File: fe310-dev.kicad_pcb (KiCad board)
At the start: 2 copper layers, 50 x 50 mm, 42 parts, among them J1 USB_B_Mini, J2 Conn_01x06, J3 Conn_01x12, J4 Conn_01x12, J5 Conn_01x08, SW1 SW_Push, U1 AMS1117-3.3, U2 AMS1117-1.8, U3 HT42B534, U4 FE310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

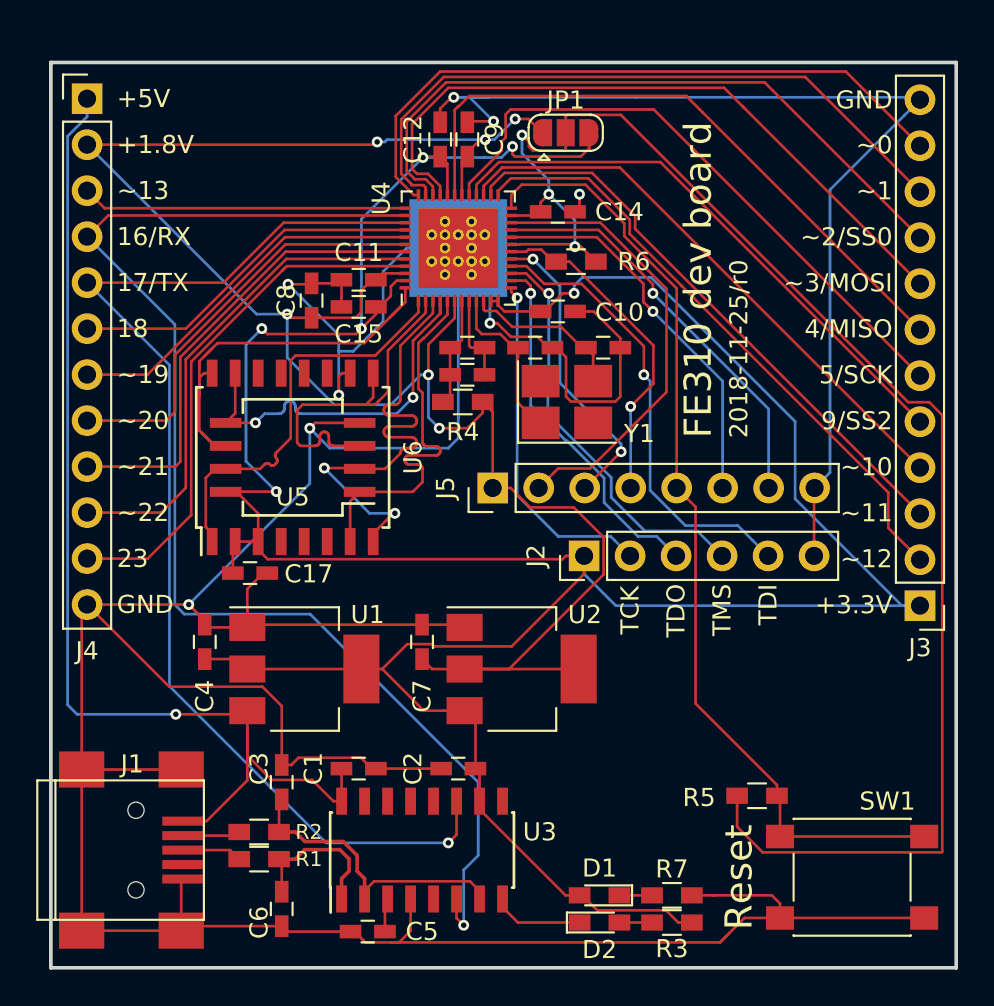
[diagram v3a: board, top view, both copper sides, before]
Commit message: various fixes and updates to silkscreen, closes #1 and #2
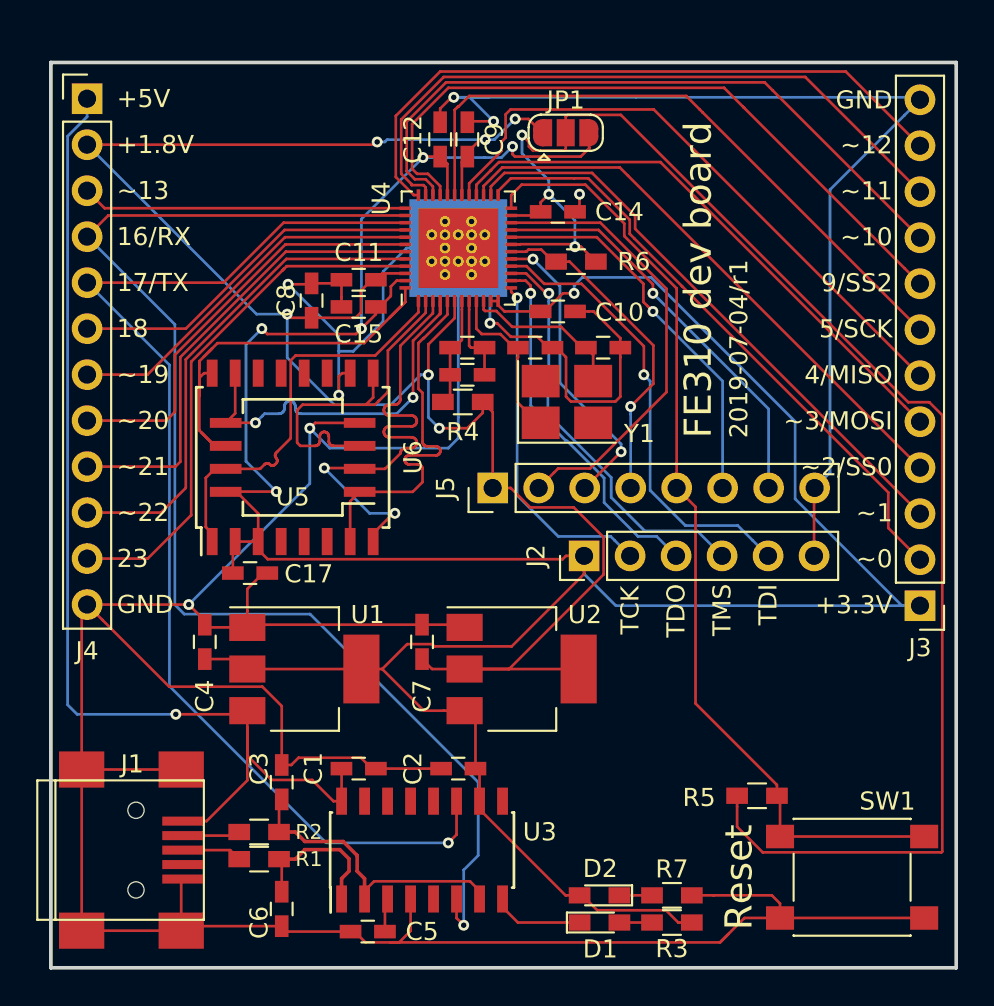
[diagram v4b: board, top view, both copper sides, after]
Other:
- board text added: "2019-07-04/r1"
- board text removed: "2018-11-25/r0"
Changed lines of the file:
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@@
     (tags "LED 0603")
     (attr smd)
-    (fp_text reference D1 (at 0 -3) (layer F.SilkS)
+    (fp_text reference D1 (at 0.039 1.467) (layer F.SilkS)
       (effects (font (size 1 1) (thickness 0.15)))
     )
@@
       (effects (font (size 1 1) (thickness 0.15)))
     )
+    (fp_line (start -1.8 -0.55) (end -1.8 0.55) (layer F.SilkS) (width 0.12))
+    (fp_line (start -0.2 -0.2) (end -0.2 0.2) (layer F.Fab) (width 0.1))
+    (fp_line (start -0.15 0) (end 0.15 -0.2) (layer F.Fab) (width 0.1))
+    (fp_line (start 0.15 0.2) (end -0.15 0) (layer F.Fab) (width 0.1))
+    (fp_line (start 0.15 -0.2) (end 0.15 0.2) (layer F.Fab) (width 0.1))
+    (fp_line (start 0.8 0.4) (end -0.8 0.4) (layer F.Fab) (width 0.1))
+    (fp_line (start 0.8 -0.4) (end 0.8 0.4) (layer F.Fab) (width 0.1))
+    (fp_line (start -0.8 -0.4) (end 0.8 -0.4) (layer F.Fab) (width 0.1))
+    (fp_line (start -1.8 0.55) (end 0.8 0.55) (layer F.SilkS) (width 0.12))
+    (fp_line (start -1.8 -0.55) (end 0.8 -0.55) (layer F.SilkS) (width 0.12))
+    (fp_line (start -1.96 -0.7) (end 1.95 -0.7) (layer F.CrtYd) (width 0.05))
+    (fp_line (start -1.96 -0.7) (end -1.96 0.7) (layer F.CrtYd) (width 0.05))
+    (fp_line (start 1.95 0.7) (end 1.95 -0.7) (layer F.CrtYd) (width 0.05))
+    (fp_line (start 1.95 0.7) (end -1.96 0.7) (layer F.CrtYd) (width 0.05))
     (fp_line (start -0.8 -0.4) (end -0.8 0.4) (layer F.Fab) (width 0.1))
-    (fp_line (start 1.95 0.7) (end -1.96 0.7) (layer F.CrtYd) (width 0.05))
-    (fp_line (start 1.95 0.7) (end 1.95 -0.7) (layer F.CrtYd) (width 0.05))
-    (fp_line (start -1.96 -0.7) (end -1.96 0.7) (layer F.CrtYd) (width 0.05))
-    (fp_line (start -1.96 -0.7) (end 1.95 -0.7) (layer F.CrtYd) (width 0.05))
-    (fp_line (start -1.8 -0.55) (end 0.8 -0.55) (layer F.SilkS) (width 0.12))
-    (fp_line (start -1.8 0.55) (end 0.8 0.55) (layer F.SilkS) (width 0.12))
-    (fp_line (start -0.8 -0.4) (end 0.8 -0.4) (layer F.Fab) (width 0.1))
-    (fp_line (start 0.8 -0.4) (end 0.8 0.4) (layer F.Fab) (width 0.1))
-    (fp_line (start 0.8 0.4) (end -0.8 0.4) (layer F.Fab) (width 0.1))
-    (fp_line (start 0.15 -0.2) (end 0.15 0.2) (layer F.Fab) (width 0.1))
-    (fp_line (start 0.15 0.2) (end -0.15 0) (layer F.Fab) (width 0.1))
-    (fp_line (start -0.15 0) (end 0.15 -0.2) (layer F.Fab) (width 0.1))
-    (fp_line (start -0.2 -0.2) (end -0.2 0.2) (layer F.Fab) (width 0.1))
-    (fp_line (start -1.8 -0.55) (end -1.8 0.55) (layer F.SilkS) (width 0.12))
+    (pad 1 smd rect (at -1.1 0) (size 1.2 0.9) (layers F.Cu F.Paste F.Mask)
+      (net 11 "Net-(D1-Pad1)"))
     (pad 2 smd rect (at 1.1 0) (size 1.2 0.9) (layers F.Cu F.Paste F.Mask)
       (net 10 "Net-(D1-Pad2)"))
-    (pad 1 smd rect (at -1.1 0) (size 1.2 0.9) (layers F.Cu F.Paste F.Mask)
-      (net 11 "Net-(D1-Pad1)"))
     (model ${KISYS3DMOD}/LEDs.3dshapes/LED_0603.wrl
       (at (xyz 0 0 0))
@@
     (tags "LED 0603")
     (attr smd)
-    (fp_text reference D2 (at 0 -3 180) (layer F.SilkS)
+    (fp_text reference D2 (at -0.039 1.478 180) (layer F.SilkS)
       (effects (font (size 1 1) (thickness 0.15)))
     )
@@
       (net 52 +VAON))
   )
-  (gr_text 2018-11-25/r0 (at 58 35.75 90) (layer F.SilkS)
+  (gr_text 2019-07-04/r1 (at 58 35.75 90) (layer F.SilkS)
     (effects (font (size 1 1) (thickness 0.25)) (justify left))
   )
@@
     (effects (font (size 1 1) (thickness 0.25)) (justify left))
   )
-  (gr_text ~~12 (at 66.486 42.418) (layer F.SilkS)
-    (effects (font (size 1 1) (thickness 0.25)) (justify right))
-  )
-  (gr_text ~~11 (at 66.486 39.878) (layer F.SilkS)
-    (effects (font (size 1 1) (thickness 0.25)) (justify right))
-  )
-  (gr_text ~~10 (at 66.486 37.338) (layer F.SilkS)
-    (effects (font (size 1 1) (thickness 0.25)) (justify right))
-  )
-  (gr_text 9/SS2 (at 66.486 34.798) (layer F.SilkS)
-    (effects (font (size 1 1) (thickness 0.25)) (justify right))
-  )
-  (gr_text 5/SCK (at 66.486 32.258) (layer F.SilkS)
-    (effects (font (size 1 1) (thickness 0.25)) (justify right))
-  )
-  (gr_text 4/MISO (at 66.486 29.718) (layer F.SilkS)
-    (effects (font (size 1 1) (thickness 0.25)) (justify right))
-  )
-  (gr_text ~~3/MOSI (at 66.486 27.178) (layer F.SilkS)
-    (effects (font (size 1 1) (thickness 0.25)) (justify right))
-  )
-  (gr_text ~~2/SS0 (at 66.486 24.638) (layer F.SilkS)
-    (effects (font (size 1 1) (thickness 0.25)) (justify right))
-  )
-  (gr_text ~~1 (at 66.486 22.098) (layer F.SilkS)
-    (effects (font (size 1 1) (thickness 0.25)) (justify right))
-  )
-  (gr_text ~~0 (at 66.486 19.558) (layer F.SilkS)
-    (effects (font (size 1 1) (thickness 0.25)) (justify right))
-  )
+  (gr_text ~~0 (at 66.486 42.418) (layer F.SilkS)
+    (effects (font (size 1 1) (thickness 0.25)) (justify right))
+  )
+  (gr_text ~~1 (at 66.486 39.878) (layer F.SilkS)
+    (effects (font (size 1 1) (thickness 0.25)) (justify right))
+  )
+  (gr_text ~~2/SS0 (at 66.486 37.338) (layer F.SilkS)
+    (effects (font (size 1 1) (thickness 0.25)) (justify right))
+  )
+  (gr_text ~~3/MOSI (at 66.486 34.798) (layer F.SilkS)
+    (effects (font (size 1 1) (thickness 0.25)) (justify right))
+  )
+  (gr_text 4/MISO (at 66.486 32.258) (layer F.SilkS)
+    (effects (font (size 1 1) (thickness 0.25)) (justify right))
+  )
+  (gr_text 5/SCK (at 66.486 29.718) (layer F.SilkS)
+    (effects (font (size 1 1) (thickness 0.25)) (justify right))
+  )
+  (gr_text 9/SS2 (at 66.486 27.178) (layer F.SilkS)
+    (effects (font (size 1 1) (thickness 0.25)) (justify right))
+  )
+  (gr_text ~~10 (at 66.486 24.638) (layer F.SilkS)
+    (effects (font (size 1 1) (thickness 0.25)) (justify right))
+  )
+  (gr_text ~~11 (at 66.486 22.098) (layer F.SilkS)
+    (effects (font (size 1 1) (thickness 0.25)) (justify right))
+  )
+  (gr_text ~~12 (at 66.486 19.558) (layer F.SilkS)
+    (effects (font (size 1 1) (thickness 0.25)) (justify right))
+  )

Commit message: add m2 mounting holes and reroute traces to accommodate (closes #3)
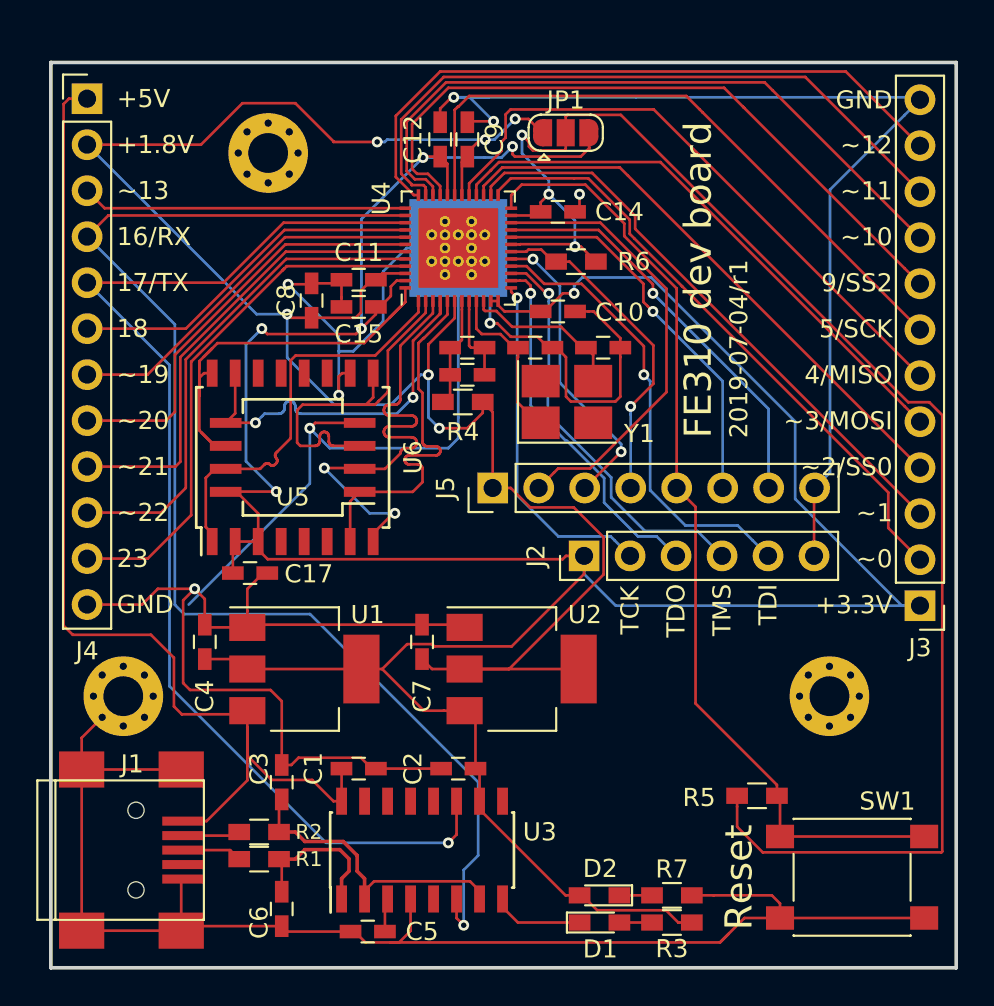
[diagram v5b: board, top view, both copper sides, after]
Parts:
- added REF**: MountingHole_2.2mm_M2_Pad_Via, MountingHole:MountingHole_2.2mm_M2_Pad_Via, F.Cu at (24.0, 50.0)
- added REF**: MountingHole_2.2mm_M2_Pad_Via, MountingHole:MountingHole_2.2mm_M2_Pad_Via, F.Cu at (63.0, 50.0)
- added REF**: MountingHole_2.2mm_M2_Pad_Via, MountingHole:MountingHole_2.2mm_M2_Pad_Via, F.Cu at (32.0, 20.0)
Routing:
- net GND: track 278.7 -> 275.1 mm
- net +1V8: track 110.3 -> 112.1 mm
- net +5V: track 62.1 -> 62.0 mm, vias 1 -> 0

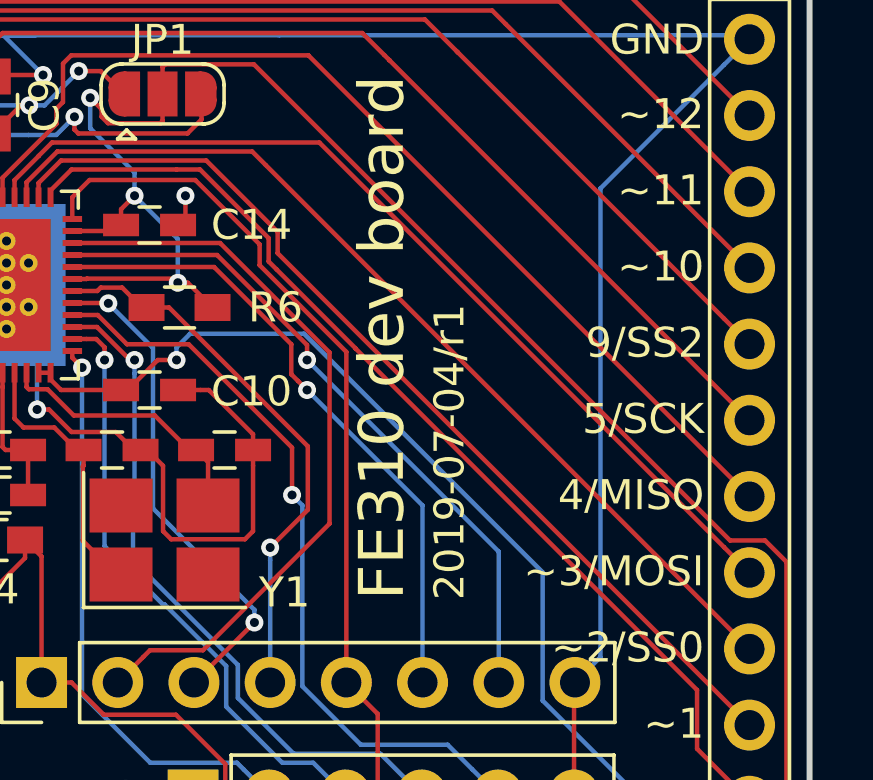
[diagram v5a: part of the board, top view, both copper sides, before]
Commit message: update date on pcb because i'm lazy and took 3 weeks before sending the board to be fabbed
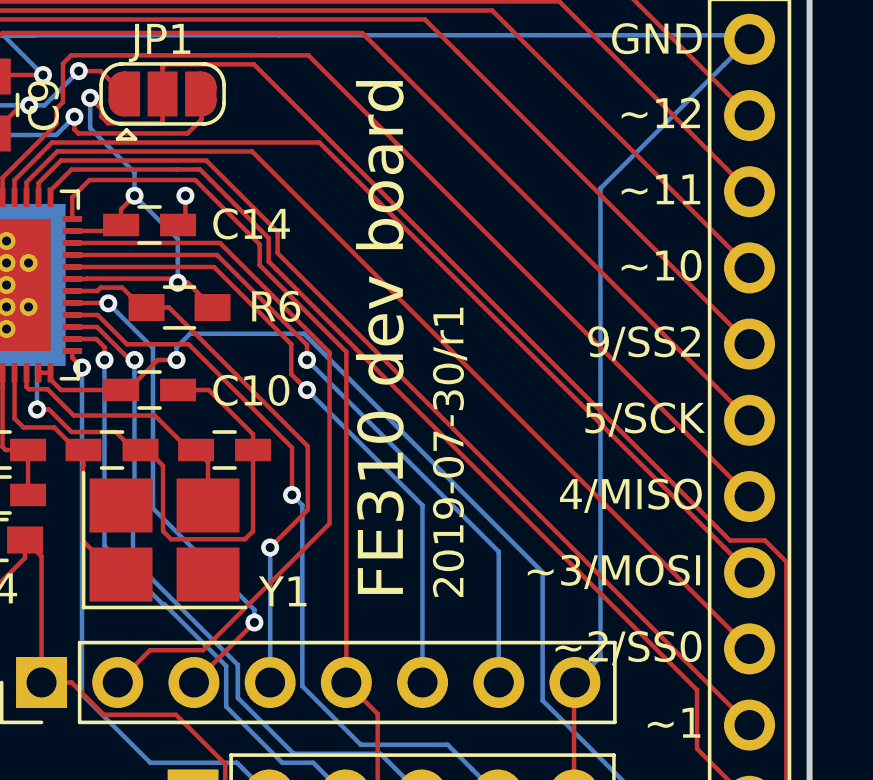
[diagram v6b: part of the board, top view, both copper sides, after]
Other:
- board text added: "2019-07-30/r1"
- board text removed: "2019-07-04/r1"
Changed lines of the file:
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@@
       (net 52 +VAON))
   )
-  (gr_text 2019-07-04/r1 (at 58 35.75 90) (layer F.SilkS)
+  (gr_text 2019-07-30/r1 (at 58 35.75 90) (layer F.SilkS)
     (effects (font (size 1 1) (thickness 0.25)) (justify left))
   )
@@
   (segment (start 42.85 48.5) (end 41.05 48.5) (width 0.15) (layer F.Cu) (net 5))
   (segment (start 42.85 48.5) (end 49.15 48.5) (width 0.15) (layer F.Cu) (net 5))
-  (segment (start 46.85 23.45) (end 47.05 23.25) (width 0.15) (layer F.Cu) (net 52))
-  (segment (start 45.425 23.45) (end 46.85 23.45) (width 0.15) (layer F.Cu) (net 52))
-  (segment (start 47.05 22.725) (end 47.5 22.275) (width 0.15) (layer F.Cu) (net 52))
-  (segment (start 47.05 23.25) (end 47.05 22.725) (width 0.15) (layer F.Cu) (net 52))
   (segment (start 42.7 20.5) (end 43 20.2) (width 0.15) (layer F.Cu) (net 5))
   (segment (start 42.7 22.325) (end 42.7 20.5) (width 0.15) (layer F.Cu) (net 5))
@@
   (segment (start 33.05 31.302002) (end 35.647999 33.900001) (width 0.15) (layer B.Cu) (net 5))
   (segment (start 33.05 28.9) (end 33.05 31.302002) (width 0.15) (layer B.Cu) (net 5))
-  (segment (start 50.1 26) (end 50.25 26) (width 0.15) (layer F.Cu) (net 52))
   (segment (start 31.36 28.9) (end 22 19.54) (width 0.15) (layer B.Cu) (net 5))
   (segment (start 33.05 28.9) (end 31.36 28.9) (width 0.15) (layer B.Cu) (net 5))
@@
   (segment (start 33.5 17.25) (end 30.58 17.25) (width 0.15) (layer F.Cu) (net 5))
   (segment (start 22 19.54) (end 28.29 19.54) (width 0.15) (layer F.Cu) (net 5))
-  (via (at 47.5 22.275) (size 0.6) (drill 0.3) (layers F.Cu B.Cu) (net 52))
   (segment (start 42.05 32.25) (end 42.05 30.75) (width 0.15) (layer F.Cu) (net 6))
   (segment (start 42.05 33.35) (end 41.65 33.75) (width 0.15) (layer F.Cu) (net 6))
@@
   (segment (start 32.75 59.15) (end 32.6 59) (width 0.15) (layer F.Cu) (net 51) (status 30))
   (segment (start 32.75 60.8) (end 32.75 59.15) (width 0.15) (layer F.Cu) (net 51) (status 30))
+  (segment (start 46.85 23.45) (end 47.05 23.25) (width 0.15) (layer F.Cu) (net 52))
+  (segment (start 45.425 23.45) (end 46.85 23.45) (width 0.15) (layer F.Cu) (net 52))
+  (segment (start 47.05 22.725) (end 47.5 22.275) (width 0.15) (layer F.Cu) (net 52))
+  (segment (start 47.05 23.25) (end 47.05 22.725) (width 0.15) (layer F.Cu) (net 52))
+  (segment (start 50.1 26) (end 50.25 26) (width 0.15) (layer F.Cu) (net 52))
+  (via (at 47.5 22.275) (size 0.6) (drill 0.3) (layers F.Cu B.Cu) (net 52))
   (segment (start 47.5 22.275) (end 47.5 21.504) (width 0.15) (layer B.Cu) (net 52))
   (segment (start 48.434 19.782) (end 48.434 18.882) (width 0.15) (layer F.Cu) (net 52))
